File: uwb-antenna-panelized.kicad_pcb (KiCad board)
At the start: 2 copper layers, 94 x 71 mm, 217 parts, among them J1 USB C, J2 Battery, J3 TC2030-NL, SW1 ~{PB}, SW2 BOOT0, SW4 ~{SR}, U1 STM6600, U2 BQ24074RGT, U3 TPS63001, U4 TPD2EUSB30, U5 STM32L432KBUx

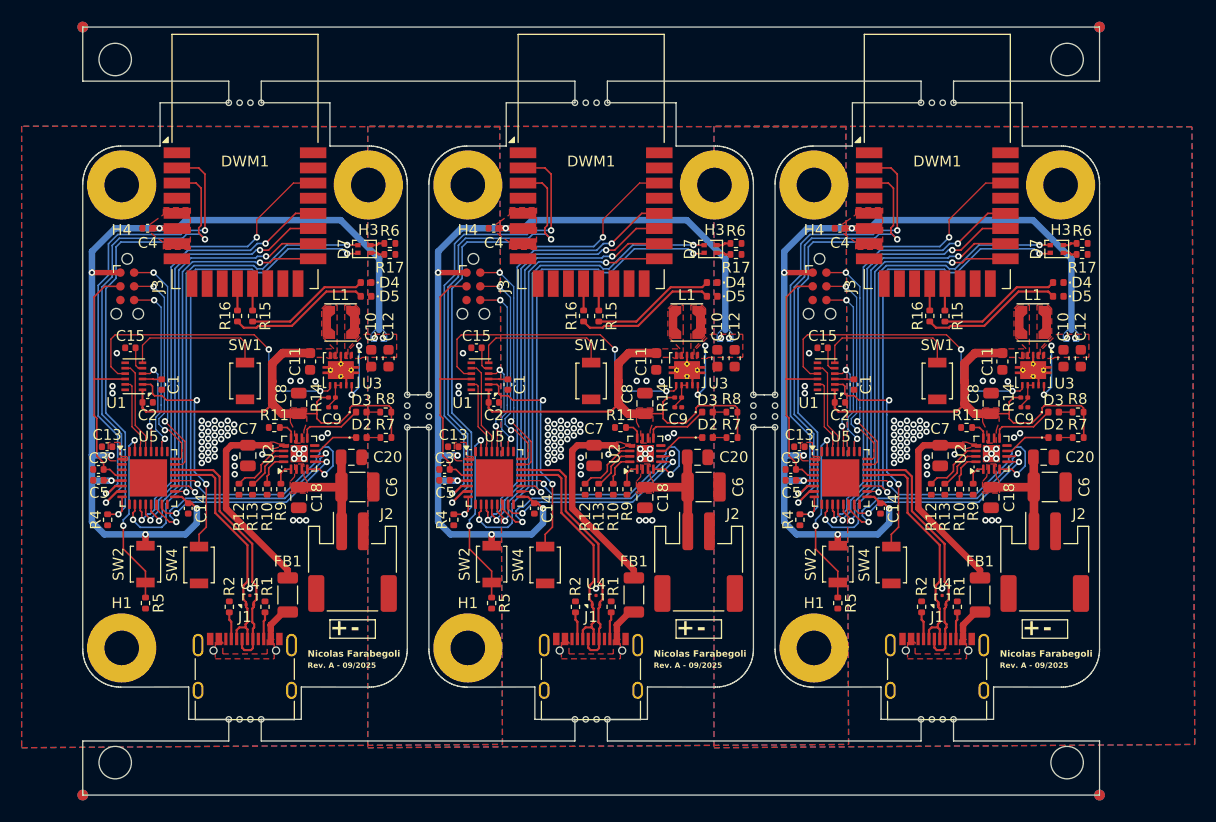
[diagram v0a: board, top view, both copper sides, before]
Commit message: feat: add panelized version
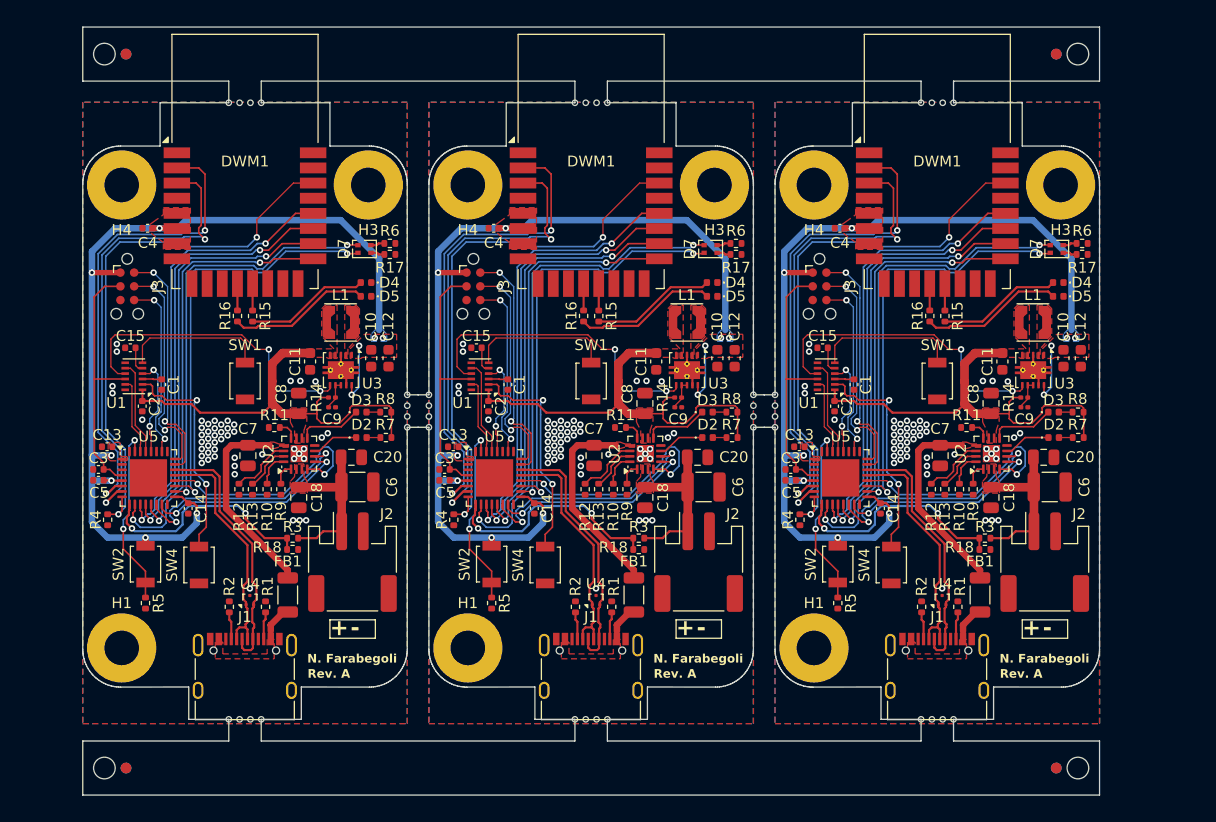
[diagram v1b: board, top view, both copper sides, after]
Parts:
- removed the C2 at (139.5, 54.7)
- removed the C2 at (171.5, 54.7)
- removed the C2 at (107.5, 54.7)
- removed the R1 at (150.3, 73.6)
- removed the R1 at (118.4, 73.6)
- removed the R1 at (182.3, 73.6)
- added C2: 0.1uF, Capacitor_SMD:C_0402_1005Metric, F.Cu at (171.0, 55.1)
- added C2: 0.1uF, Capacitor_SMD:C_0402_1005Metric, F.Cu at (139.0, 55.1)
- added C2: 0.1uF, Capacitor_SMD:C_0402_1005Metric, F.Cu at (107.0, 55.1)
- added R1: 5.1K, Resistor_SMD:R_0402_1005Metric, F.Cu at (150.4, 73.6)
- added R1: 5.1K, Resistor_SMD:R_0402_1005Metric, F.Cu at (118.4, 73.6)
- added R1: 5.1K, Resistor_SMD:R_0402_1005Metric, F.Cu at (182.4, 73.6)
- added R18: 20K, Resistor_SMD:R_0402_1005Metric, F.Cu at (152.9, 68.3)
- added R18: 20K, Resistor_SMD:R_0402_1005Metric, F.Cu at (120.9, 68.3)
- added R18: 20K, Resistor_SMD:R_0402_1005Metric, F.Cu at (184.9, 68.3)
- added R3: 10K, Resistor_SMD:R_0402_1005Metric, F.Cu at (152.9, 67.3)
- added R3: 10K, Resistor_SMD:R_0402_1005Metric, F.Cu at (184.9, 67.3)
- added R3: 10K, Resistor_SMD:R_0402_1005Metric, F.Cu at (120.9, 67.3)
- moved KiKit_FID_B_1 4.72 mm to (105.5, 22.5)
- moved KiKit_FID_B_2 4.72 mm to (191.5, 22.5)
- moved KiKit_FID_B_3 4.72 mm to (105.5, 88.5)
- moved KiKit_FID_B_4 4.72 mm to (191.5, 88.5)
- moved KiKit_FID_T_1 4.72 mm to (105.5, 22.5)
- moved KiKit_FID_T_2 4.72 mm to (191.5, 22.5)
- moved KiKit_FID_T_3 4.72 mm to (105.5, 88.5)
- moved KiKit_FID_T_4 4.72 mm to (191.5, 88.5)
- moved KiKit_TO_1 1.12 mm to (103.5, 22.5)
- moved KiKit_TO_2 1.12 mm to (193.5, 22.5)
- moved KiKit_TO_3 1.12 mm to (103.5, 88.5)
- moved KiKit_TO_4 1.12 mm to (193.5, 88.5)
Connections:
- U5 pad 9: Board_0-unconnected-(U5-PA3-Pad9) -> Board_0-/BATT_READ
- U5 pad 9: Board_1-unconnected-(U5-PA3-Pad9) -> Board_1-/BATT_READ
- U5 pad 9: Board_2-unconnected-(U5-PA3-Pad9) -> Board_2-/BATT_READ
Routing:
- net Board_0-/BATT_READ: track 0.00 -> 21.2 mm, vias 0 -> 2
- net Board_2-/BATT_READ: track 0.00 -> 21.2 mm, vias 0 -> 2
- net Board_1-/BATT_READ: track 0.00 -> 21.2 mm, vias 0 -> 2
- net Board_2-/BAT: track 10.8 -> 15.1 mm
- net Board_1-/BAT: track 10.8 -> 15.1 mm
- net Board_0-/BAT: track 10.8 -> 15.1 mm
- net Board_2-/SWCLK: track 20.2 -> 20.7 mm
- net Board_1-/SWCLK: track 20.2 -> 20.7 mm
- net Board_0-/SWCLK: track 20.2 -> 20.7 mm
- net Board_2-GND: vias 48 -> 50
- net Board_1-GND: vias 48 -> 50
- net Board_0-GND: vias 48 -> 50
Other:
- board text added: "N. Farabegoli"
- board text added: "Rev. A"
- board text removed: "Nicolas Farabegoli"
- board text removed: "Rev. A - 09/2025"
